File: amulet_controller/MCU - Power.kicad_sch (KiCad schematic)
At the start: 13 parts, among them U1 STM32G474RET3

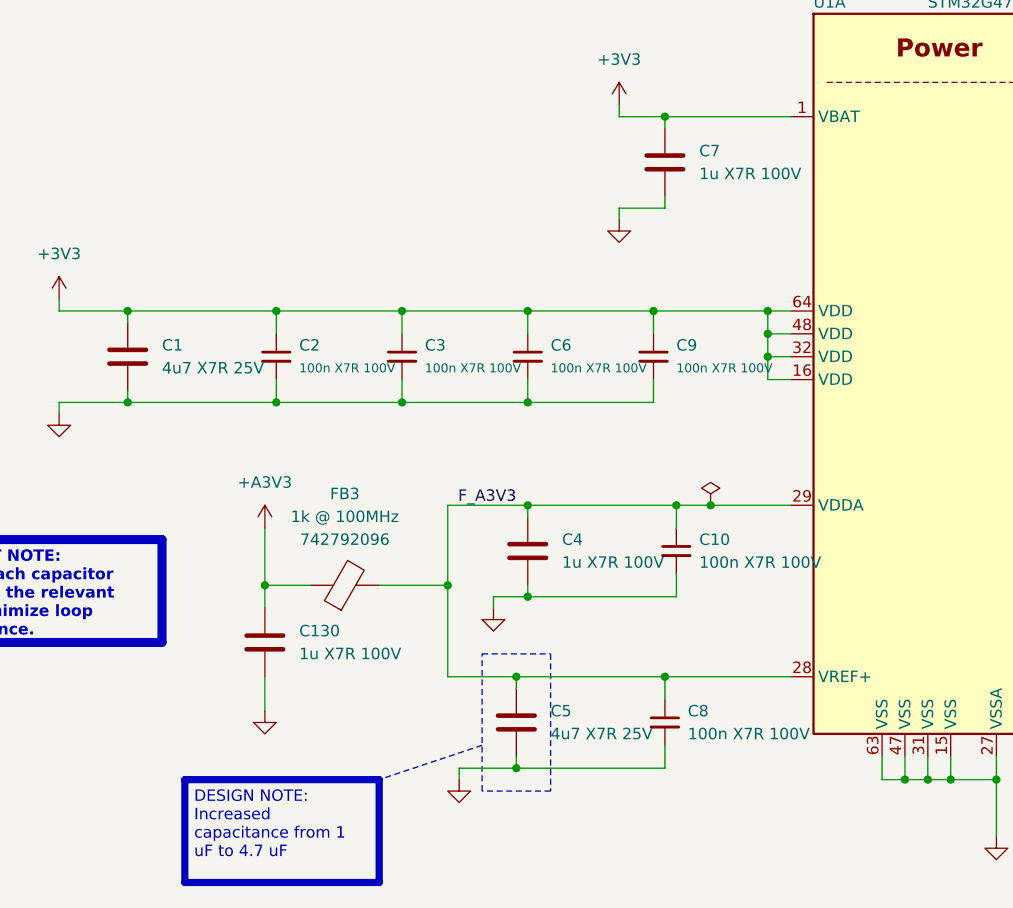
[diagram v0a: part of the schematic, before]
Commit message: filled in fields for bom, replaced inexisting components. Need to replace LEDs
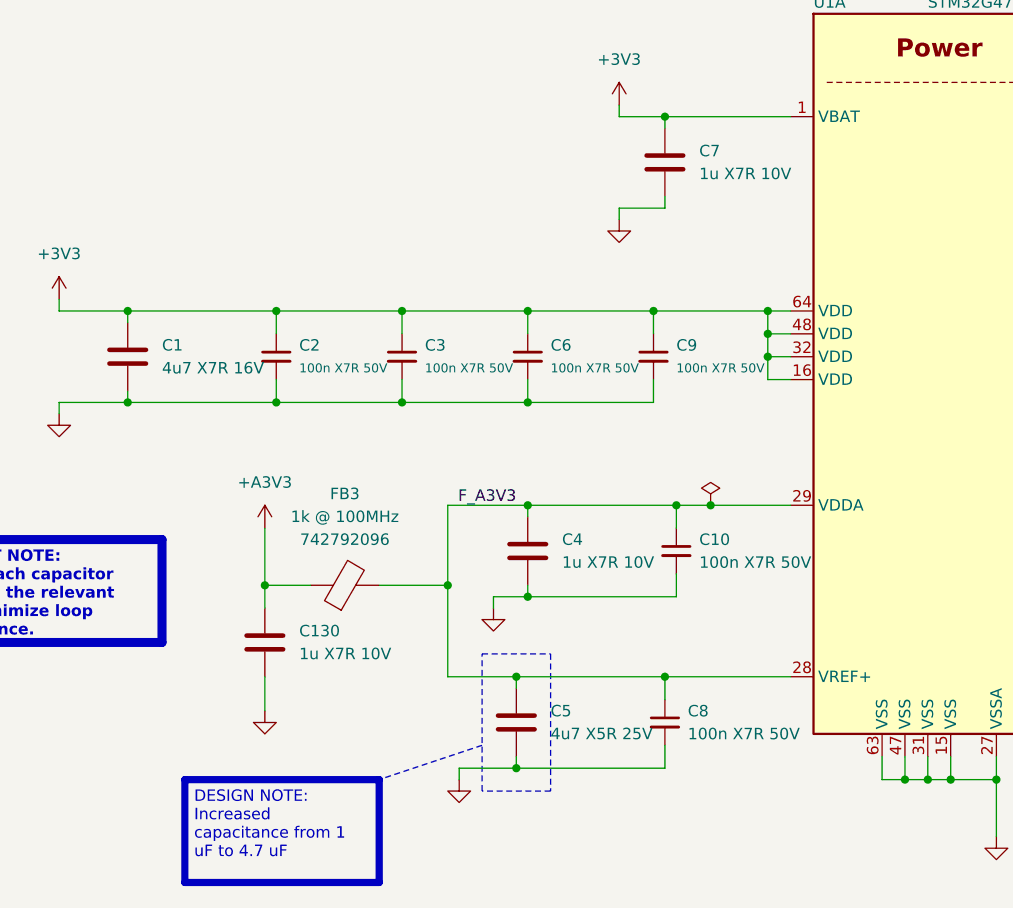
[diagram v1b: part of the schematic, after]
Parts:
- C1: value 4u7 X7R 25V -> 4u7 X7R 16V; Manufacturer (none) -> Murata Electronics; Manufacturer Part Number (none) -> GRM188Z71C475KE21J; Supplier 1 (none) -> Digikey; Supplier Part Number 1 (none) -> 490-GRM188Z71C475KE21JCT-ND
- C10, C2, C3, C6, C8, C9: value 100n X7R 100V -> 100n X7R 50V; Manufacturer (none) -> Murata Electronics; Manufacturer Part Number (none) -> GCM155R71H104KE02J; Supplier 1 (none) -> Digikey; Supplier Part Number 1 (none) -> 490-14514-1-ND
- C130, C4, C7: value 1u X7R 100V -> 1u X7R 10V; Manufacturer (none) -> Murata Electronics; Manufacturer Part Number (none) -> GRM155Z71A105KE01J; Supplier 1 (none) -> Digikey; Supplier Part Number 1 (none) -> 490-GRM155Z71A105KE01JCT-ND
- C5: value 4u7 X7R 25V -> 4u7 X5R 25V; Manufacturer (none) -> KYOCERA AVX; Manufacturer Part Number (none) -> 04023D475MAT2A; Supplier 1 (none) -> Digikey; Supplier Part Number 1 (none) -> 478-04023D475MAT2ACT-ND
- FB3: Manufacturer (none) -> Würth Elektronik; Supplier 1 (none) -> Digikey; Supplier Part Number 1 (none) -> 732-4648-1-ND
- U1: Manufacturer (none) -> STMicroelectronics; Manufacturer Part Number (none) -> STM32G474RET3; Supplier 1 (none) -> Digikey; Supplier Part Number 1 (none) -> 497-STM32G474RET3-ND

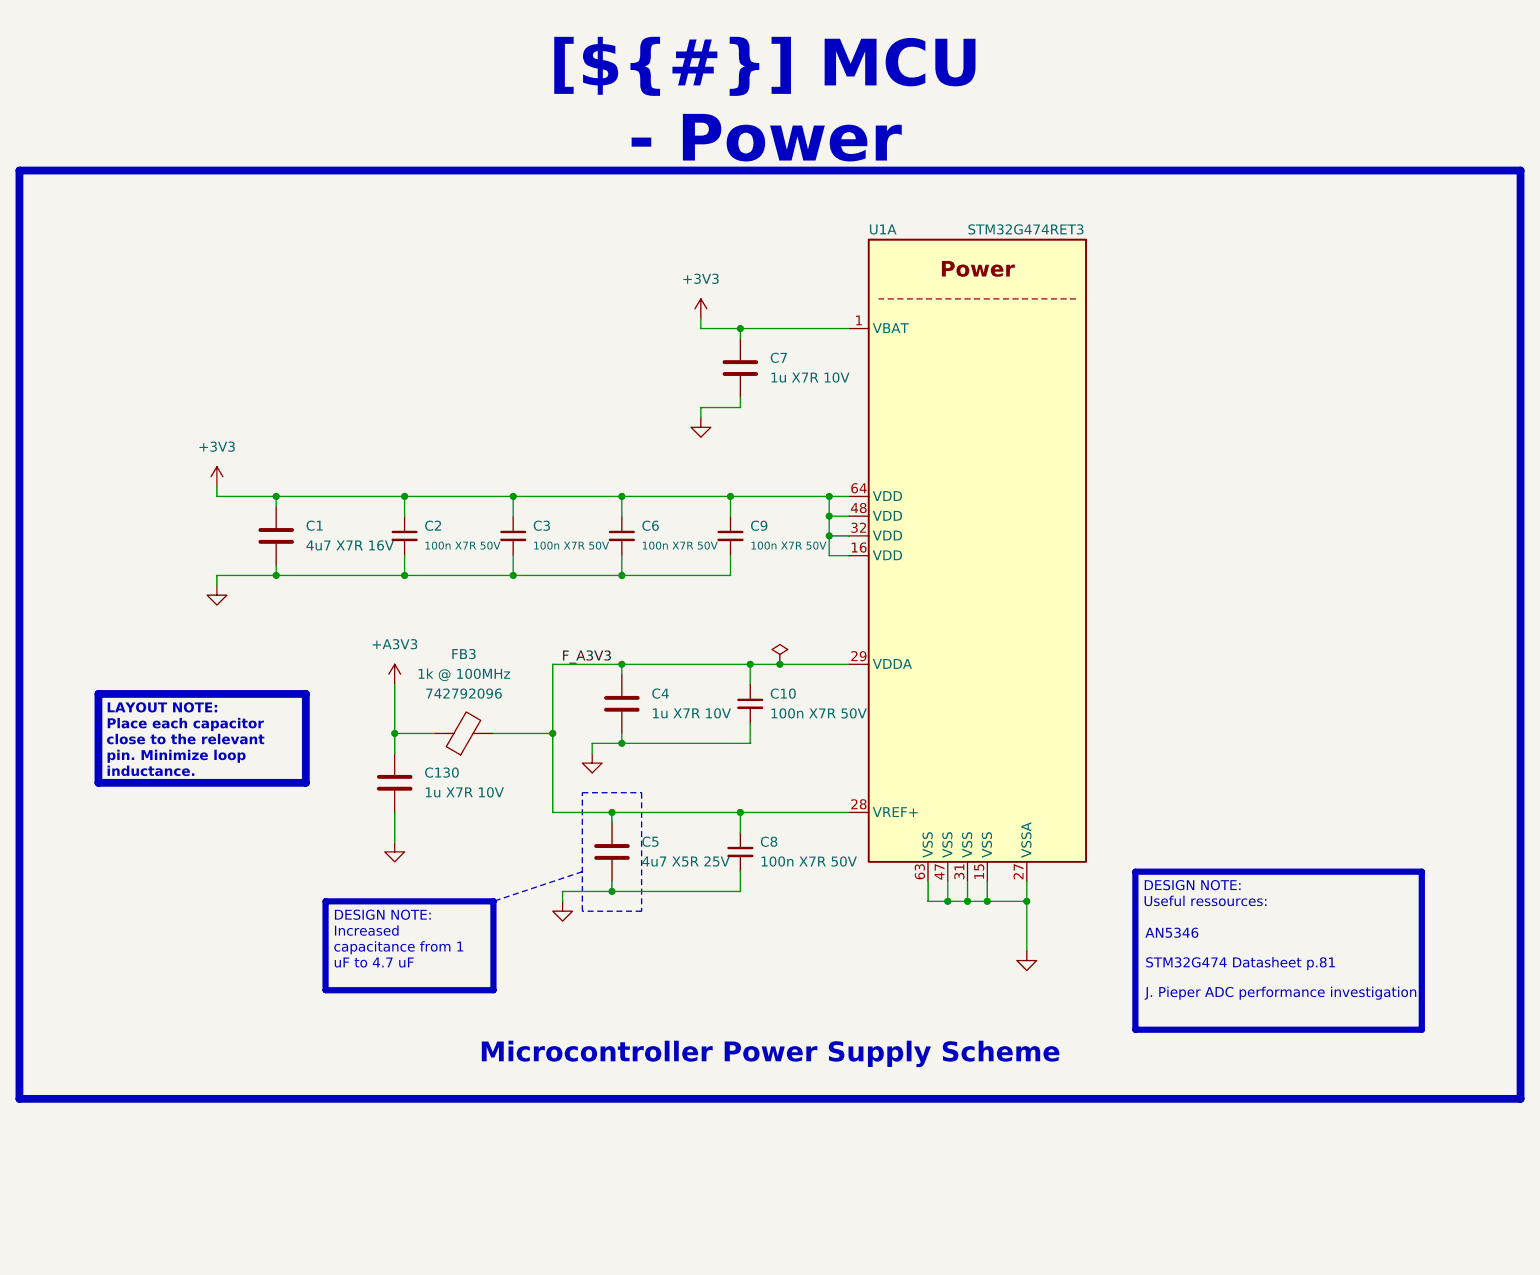
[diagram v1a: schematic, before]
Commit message: finalized pcb. TODO: add clean BOM and KiBot integration
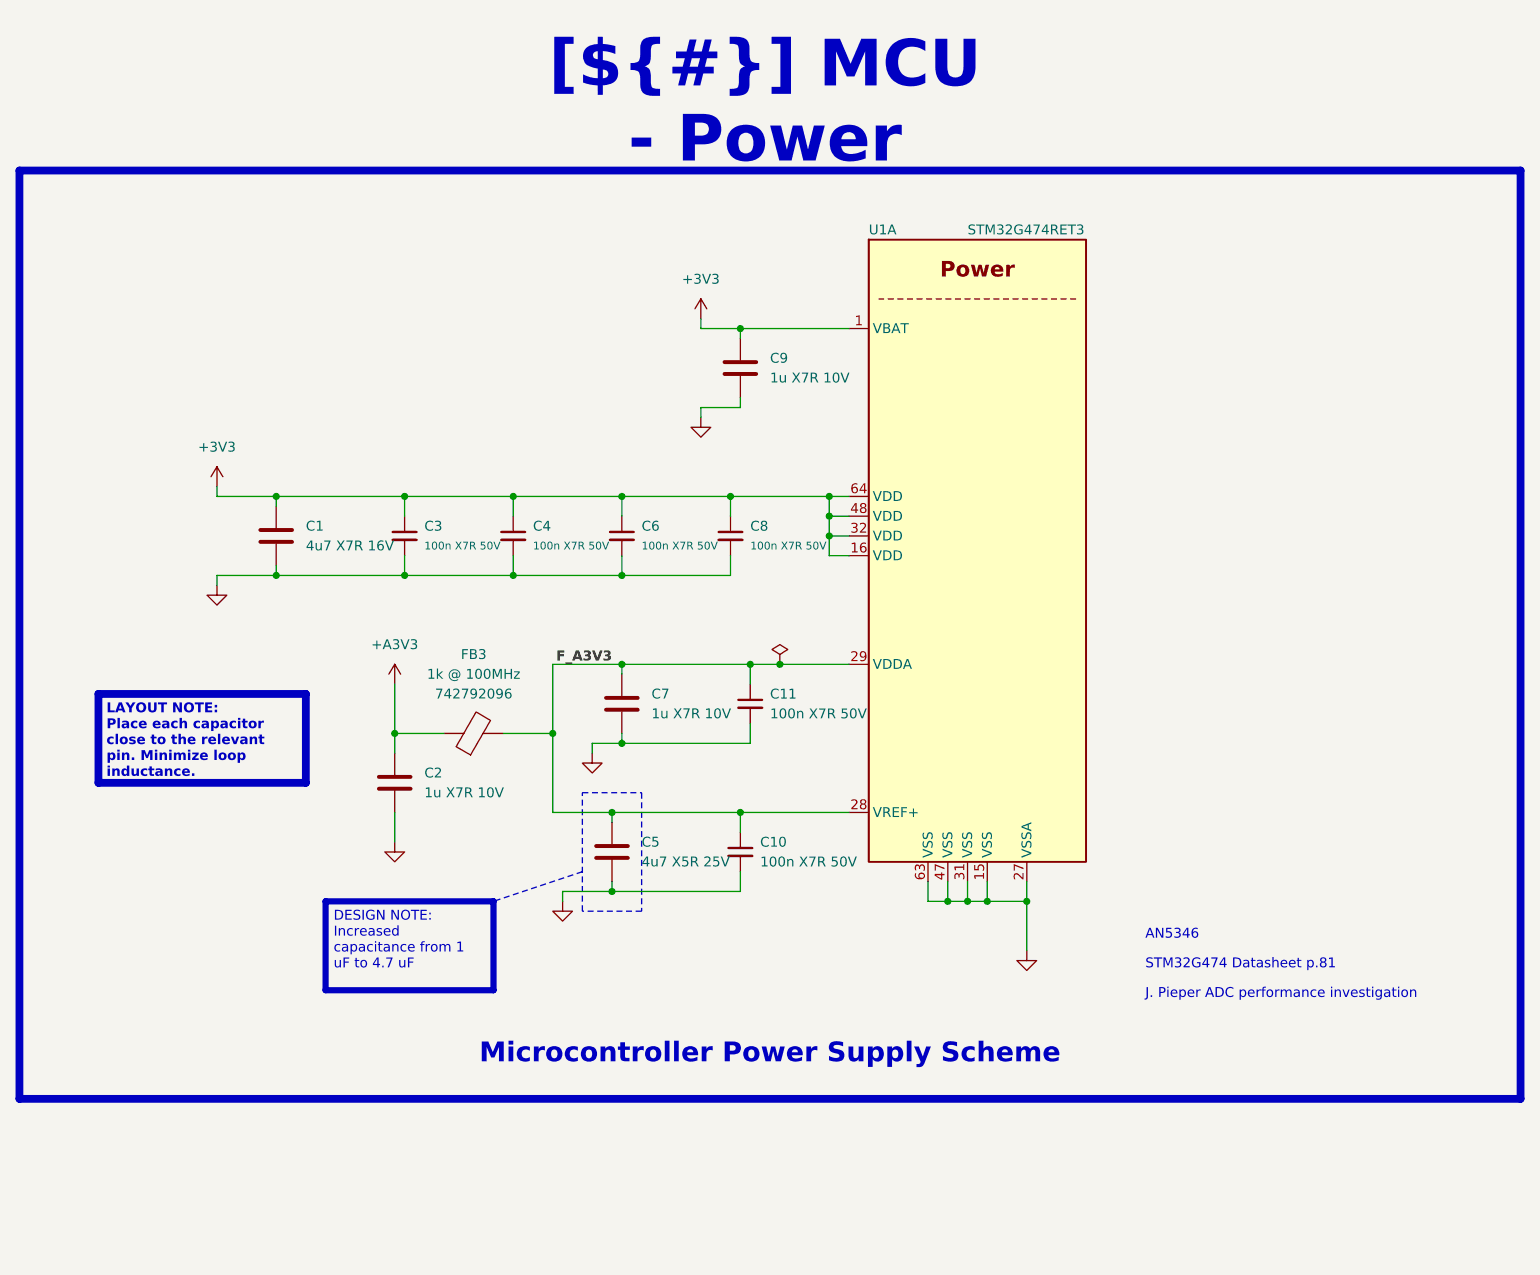
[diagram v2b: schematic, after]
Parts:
- renumbered C8 to C10, C10 to C11, C130 to C2, C2 to C3, C3 to C4, C4 to C7, C9 to C8, C7 to C9
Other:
- moved on the sheet: FB3

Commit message: minor updates
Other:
- note added: "J. Pieper ADC investigation"
- note removed: "J. Pieper ADC performance investigation"
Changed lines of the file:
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@@
     (effects (font (face "Arial") (size 1.27 1.27) (color 0 0 0 1)) (justify left top))
   )
-  (text "J. Pieper ADC performance investigation" (at 200.66 137.16 0)
+  (text "J. Pieper ADC investigation" (at 142.24 170.18 0)
     (effects (font (face "Arial") (size 1.27 1.27) (color 0 0 0 1)) (justify left bottom) (href "https://jpieper.com/2023/07/24/stm32g4-adc-performance-part-2/"))
   )
-  (text "STM32G474 Datasheet p.81" (at 200.66 133.35 0)
+  (text "STM32G474 Datasheet p.81" (at 142.24 166.37 0)
     (effects (font (face "Arial") (size 1.27 1.27) (color 0 0 0 1)) (justify left bottom) (href "https://www.st.com/resource/en/datasheet/stm32g474cb.pdf"))
   )
-  (text "AN5346" (at 200.66 129.54 0)
+  (text "AN5346" (at 142.24 162.56 0)
     (effects (font (face "Arial") (size 1.27 1.27) (color 0 0 0 1)) (justify left bottom) (href "https://www.st.com/resource/en/application_note/an5346-stm32g4-adc-use-tips-and-recommendations-stmicroelectronics.pdf"))
   )

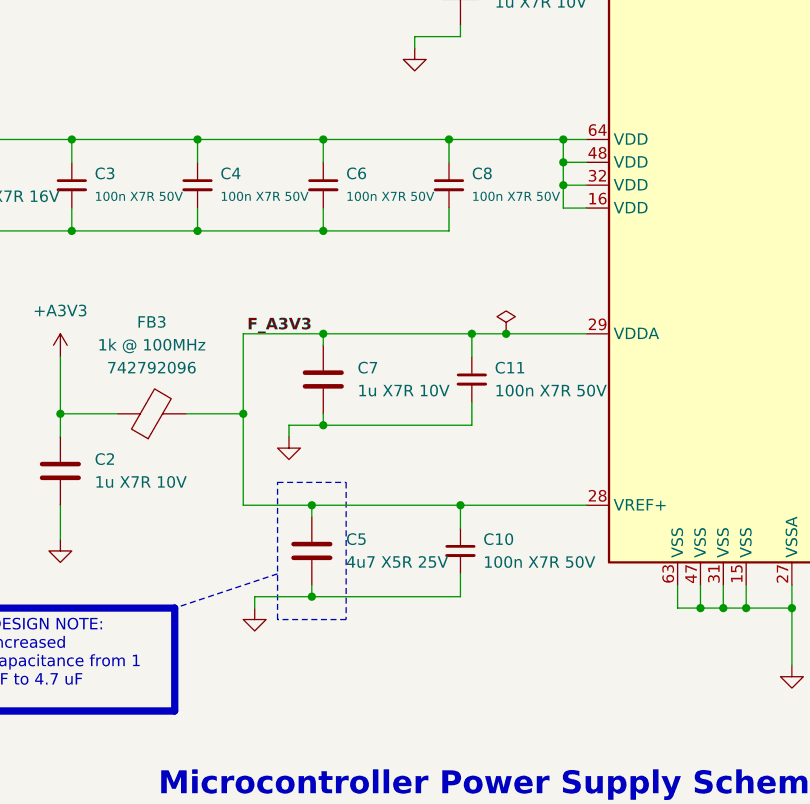
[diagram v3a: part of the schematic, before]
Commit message: corrected pcb according to reviews on reddit
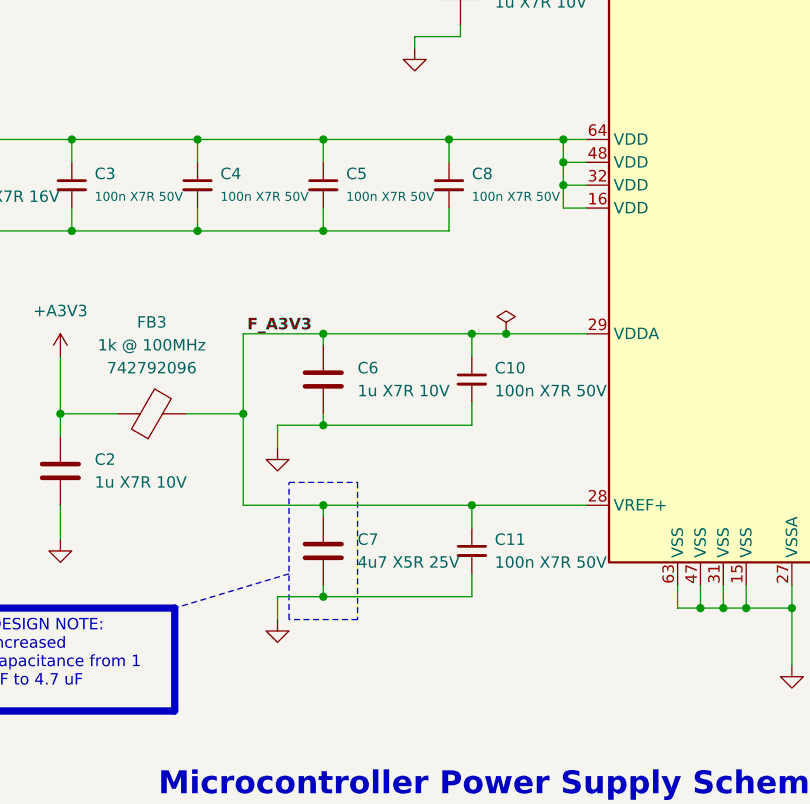
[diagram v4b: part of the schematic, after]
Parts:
- renumbered C11 to C10, C10 to C11, C6 to C5, C7 to C6, C5 to C7
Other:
- moved on the sheet: C11, C7
